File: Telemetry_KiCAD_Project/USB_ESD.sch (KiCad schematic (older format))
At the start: 9 parts

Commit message: Annotated Components
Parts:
- gave numbers to parts that had none: 9
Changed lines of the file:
@@
 $EndDescr
 $Comp
-L dk_USB-DVI-HDMI-Connectors:10118192-0001LF J?
+L dk_USB-DVI-HDMI-Connectors:10118192-0001LF J3
 U 1 1 61A3682F
 P 2500 3450
-F 0 "J?" H 2564 4195 60  0000 C CNN
+F 0 "J3" H 2564 4195 60  0000 C CNN
 F 1 "10118192-0001LF" H 2564 4089 60  0000 C CNN
 F 2 "digikey-footprints:USB_Micro_B_Female_10118192" H 2700 3650 60  0001 L CNN
@@
 $EndComp
 $Comp
-L dk_PMIC-Voltage-Regulators-Linear:LM317T U?
+L dk_PMIC-Voltage-Regulators-Linear:LM317T U6
 U 1 1 61A380E7
 P 5500 3250
-F 0 "U?" H 5500 3537 60  0000 C CNN
+F 0 "U6" H 5500 3537 60  0000 C CNN
 F 1 "LM317T" H 5500 3431 60  0000 C CNN
 F 2 "digikey-footprints:TO-220-3" H 5700 3450 60  0001 L CNN
@@
 $EndComp
 $Comp
-L Device:R_Small R?
+L Device:R_Small R7
 U 1 1 61A38BFA
 P 5500 3800
-F 0 "R?" H 5559 3846 50  0000 L CNN
+F 0 "R7" H 5559 3846 50  0000 L CNN
 F 1 "390Ω" H 5559 3755 50  0000 L CNN
 F 2 "" H 5500 3800 50  0001 C CNN
@@
 $EndComp
 $Comp
-L Device:R_Small R?
+L Device:R_Small R8
 U 1 1 61A38F8D
 P 5900 3450
-F 0 "R?" H 5959 3496 50  0000 L CNN
+F 0 "R8" H 5959 3496 50  0000 L CNN
 F 1 "240Ω" H 5959 3405 50  0000 L CNN
 F 2 "" H 5900 3450 50  0001 C CNN
@@
 $EndComp
 $Comp
-L Device:C_Small C?
+L Device:C_Small C28
 U 1 1 61A3935C
 P 6300 3450
-F 0 "C?" H 6392 3496 50  0000 L CNN
+F 0 "C28" H 6392 3496 50  0000 L CNN
 F 1 "1uF" H 6392 3405 50  0000 L CNN
 F 2 "" H 6300 3450 50  0001 C CNN
@@
 $EndComp
 $Comp
-L Device:C_Small C?
+L Device:C_Small C27
 U 1 1 61A394F0
 P 5000 3500
-F 0 "C?" H 5092 3546 50  0000 L CNN
+F 0 "C27" H 5092 3546 50  0000 L CNN
 F 1 "0.1uF" H 5092 3455 50  0000 L CNN
 F 2 "" H 5000 3500 50  0001 C CNN
@@
 $EndComp
 $Comp
-L power:GND #PWR?
+L power:GND #PWR0140
 U 1 1 61A3A615
 P 6300 3550
-F 0 "#PWR?" H 6300 3300 50  0001 C CNN
+F 0 "#PWR0140" H 6300 3300 50  0001 C CNN
 F 1 "GND" H 6305 3377 50  0000 C CNN
 F 2 "" H 6300 3550 50  0001 C CNN
@@
 $EndComp
 $Comp
-L power:+3.3V #PWR?
+L power:+3.3V #PWR0141
 U 1 1 61A3A807
 P 6100 2950
-F 0 "#PWR?" H 6100 2800 50  0001 C CNN
+F 0 "#PWR0141" H 6100 2800 50  0001 C CNN
 F 1 "+3.3V" H 6115 3123 50  0000 C CNN
 F 2 "" H 6100 2950 50  0001 C CNN
@@
 $EndComp
 $Comp
-L power:GND #PWR?
+L power:GND #PWR0142
 U 1 1 61A3A937
 P 2900 3700
-F 0 "#PWR?" H 2900 3450 50  0001 C CNN
+F 0 "#PWR0142" H 2900 3450 50  0001 C CNN
 F 1 "GND" H 2905 3527 50  0000 C CNN
 F 2 "" H 2900 3700 50  0001 C CNN
@@
 NoConn ~ 2800 3550
 $Comp
-L Device:D_Schottky_Small D?
+L Device:D_Schottky_Small D1
 U 1 1 61A3A235
 P 4700 3250
-F 0 "D?" H 4700 3455 50  0000 C CNN
+F 0 "D1" H 4700 3455 50  0000 C CNN
 F 1 "D_Schottky_Small" H 4700 3364 50  0000 C CNN
 F 2 "" V 4700 3250 50  0001 C CNN
@@
 Connection ~ 5900 3250
 $Comp
-L power:GND #PWR?
+L power:GND #PWR0143
 U 1 1 61A45748
 P 5000 3600
-F 0 "#PWR?" H 5000 3350 50  0001 C CNN
+F 0 "#PWR0143" H 5000 3350 50  0001 C CNN
 F 1 "GND" H 5005 3427 50  0000 C CNN
 F 2 "" H 5000 3600 50  0001 C CNN
@@
 $EndComp
 $Comp
-L power:GND #PWR?
+L power:GND #PWR0144
 U 1 1 61A459EF
 P 5500 3900
-F 0 "#PWR?" H 5500 3650 50  0001 C CNN
+F 0 "#PWR0144" H 5500 3650 50  0001 C CNN
 F 1 "GND" H 5505 3727 50  0000 C CNN
 F 2 "" H 5500 3900 50  0001 C CNN
@@
 	6100 3250 5900 3250
 $Comp
-L power:+5V #PWR?
+L power:+5V #PWR0145
 U 1 1 61A4867E
 P 5000 2950
-F 0 "#PWR?" H 5000 2800 50  0001 C CNN
+F 0 "#PWR0145" H 5000 2800 50  0001 C CNN
 F 1 "+5V" H 5015 3123 50  0000 C CNN
 F 2 "" H 5000 2950 50  0001 C CNN
@@
 	5000 2950 5000 3250
 $Comp
-L Device:Ferrite_Bead_Small FB?
+L Device:Ferrite_Bead_Small FB1
 U 1 1 61A399BC
 P 3800 3250
-F 0 "FB?" V 3563 3250 50  0000 C CNN
+F 0 "FB1" V 3563 3250 50  0000 C CNN
 F 1 "Ferrite_Bead_Small" V 3654 3250 50  0000 C CNN
 F 2 "" V 3730 3250 50  0001 C CNN
@@
 USB_CONN_D-
 $Comp
-L Power_Protection:USBLC6-2SC6 U?
+L Power_Protection:USBLC6-2SC6 U7
 U 1 1 61A51E77
 P 8650 3800
-F 0 "U?" H 8900 4150 50  0000 C CNN
+F 0 "U7" H 8900 4150 50  0000 C CNN
 F 1 "USBLC6-2SC6" H 9000 3500 50  0000 C CNN
 F 2 "Package_TO_SOT_SMD:SOT-23-6" H 7900 4200 50  0001 C CNN
@@
 $EndComp
 $Comp
-L power:+5V #PWR?
+L power:+5V #PWR0146
 U 1 1 61A531CE
 P 8650 3300
-F 0 "#PWR?" H 8650 3150 50  0001 C CNN
+F 0 "#PWR0146" H 8650 3150 50  0001 C CNN
 F 1 "+5V" H 8665 3473 50  0000 C CNN
 F 2 "" H 8650 3300 50  0001 C CNN
@@
 D+
 $Comp
-L power:GND #PWR?
+L power:GND #PWR0147
 U 1 1 61A5476E
 P 8650 4300
-F 0 "#PWR?" H 8650 4050 50  0001 C CNN
+F 0 "#PWR0147" H 8650 4050 50  0001 C CNN
 F 1 "GND" H 8655 4127 50  0000 C CNN
 F 2 "" H 8650 4300 50  0001 C CNN

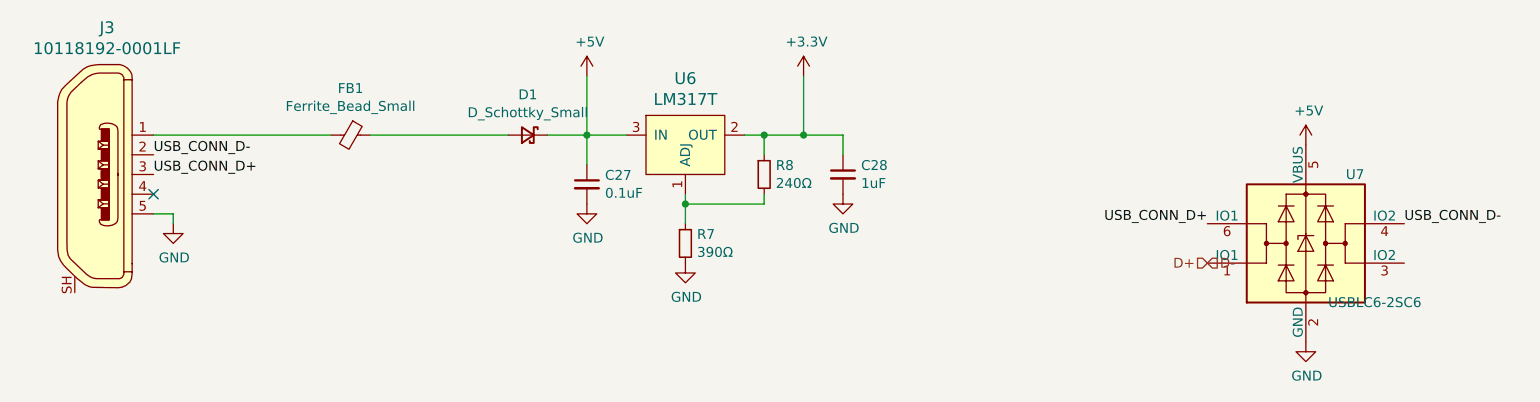
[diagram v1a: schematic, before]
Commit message: Corrected hierarchical pin directions, squashed bugs
There are still some warnings about pins being connected but not driven, don't know how to fix those at the moment
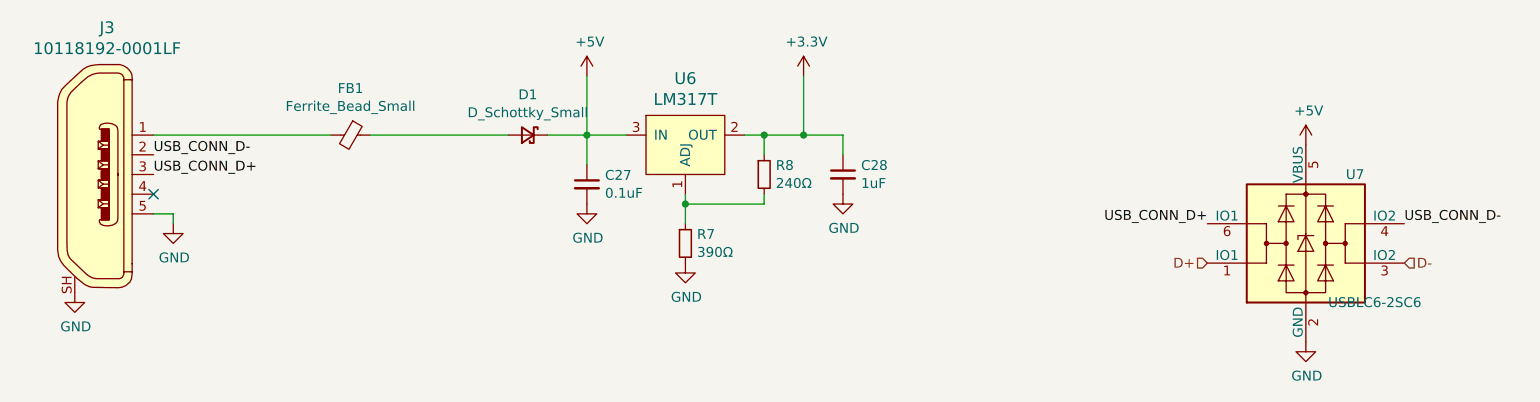
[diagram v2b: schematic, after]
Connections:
- net GND: now also J3.SH
- net D-: now reaches U7.3 (IO2)
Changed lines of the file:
@@
 $Descr A4 11693 8268
 encoding utf-8
-Sheet 8 8
+Sheet 6 8
 Title ""
 Date ""
@@
 Text Label 9150 3700 0    50   ~ 0
 USB_CONN_D-
-Text HLabel 8150 3900 2    50   Input ~ 0
+Text HLabel 9150 3900 2    50   Input ~ 0
 D-
 Text HLabel 8150 3900 0    50   Input ~ 0
@@
 	1    0    0    -1
 $EndComp
+$Comp
+L power:GND #PWR0139
+U 1 1 61A8CA77
+P 2400 4050
+F 0 "#PWR0139" H 2400 3800 50  0001 C CNN
+F 1 "GND" H 2405 3877 50  0000 C CNN
+F 2 "" H 2400 4050 50  0001 C CNN
+F 3 "" H 2400 4050 50  0001 C CNN
+	1    2400 4050
+	1    0    0    -1
+$EndComp

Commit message: Assigned footprints to all components (except duplexer)
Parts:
- C27, C28, FB1: footprint (none) -> Capacitor_SMD:C_0603_1608Metric
- D1: footprint (none) -> Diode_SMD:D_0201_0603Metric
- R7, R8: footprint (none) -> Resistor_SMD:R_0201_0603Metric
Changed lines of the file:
@@
 F 0 "R7" H 5559 3846 50  0000 L CNN
 F 1 "390Ω" H 5559 3755 50  0000 L CNN
-F 2 "" H 5500 3800 50  0001 C CNN
+F 2 "Resistor_SMD:R_0201_0603Metric" H 5500 3800 50  0001 C CNN
 F 3 "~" H 5500 3800 50  0001 C CNN
 	1    5500 3800
@@
 F 0 "R8" H 5959 3496 50  0000 L CNN
 F 1 "240Ω" H 5959 3405 50  0000 L CNN
-F 2 "" H 5900 3450 50  0001 C CNN
+F 2 "Resistor_SMD:R_0201_0603Metric" H 5900 3450 50  0001 C CNN
 F 3 "~" H 5900 3450 50  0001 C CNN
 	1    5900 3450
@@
 F 0 "C28" H 6392 3496 50  0000 L CNN
 F 1 "1uF" H 6392 3405 50  0000 L CNN
-F 2 "" H 6300 3450 50  0001 C CNN
+F 2 "Capacitor_SMD:C_0603_1608Metric" H 6300 3450 50  0001 C CNN
 F 3 "~" H 6300 3450 50  0001 C CNN
 	1    6300 3450
@@
 F 0 "C27" H 5092 3546 50  0000 L CNN
 F 1 "0.1uF" H 5092 3455 50  0000 L CNN
-F 2 "" H 5000 3500 50  0001 C CNN
+F 2 "Capacitor_SMD:C_0603_1608Metric" H 5000 3500 50  0001 C CNN
 F 3 "~" H 5000 3500 50  0001 C CNN
 	1    5000 3500
@@
 F 0 "D1" H 4700 3455 50  0000 C CNN
 F 1 "D_Schottky_Small" H 4700 3364 50  0000 C CNN
-F 2 "" V 4700 3250 50  0001 C CNN
+F 2 "Diode_SMD:D_0201_0603Metric" V 4700 3250 50  0001 C CNN
 F 3 "~" V 4700 3250 50  0001 C CNN
 	1    4700 3250
@@
 F 0 "FB1" V 3563 3250 50  0000 C CNN
 F 1 "Ferrite_Bead_Small" V 3654 3250 50  0000 C CNN
-F 2 "" V 3730 3250 50  0001 C CNN
+F 2 "Capacitor_SMD:C_0603_1608Metric" V 3730 3250 50  0001 C CNN
 F 3 "~" H 3800 3250 50  0001 C CNN
 	1    3800 3250

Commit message: Assigned capacitors for new MCU
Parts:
- U7: symbol Power_Protection:USBLC6-2SC6 -> Telemetry_KiCAD_Project-rescue:USBLC6-2SC6-Power_Protection
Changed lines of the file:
@@
 EESchema Schematic File Version 4
-LIBS:Telemetry_KiCAD_Project-cache
-EELAYER 29 0
+EELAYER 30 0
 EELAYER END
 $Descr A4 11693 8268
@@
 USB_CONN_D-
 $Comp
-L Power_Protection:USBLC6-2SC6 U7
+L Telemetry_KiCAD_Project-rescue:USBLC6-2SC6-Power_Protection U7
 U 1 1 61A51E77
 P 8650 3800
+AR Path="/61A51E77" Ref="U7"  Part="1"
+AR Path="/61A2ED84/61A51E77" Ref="U7"  Part="1"
 F 0 "U7" H 8900 4150 50  0000 C CNN
 F 1 "USBLC6-2SC6" H 9000 3500 50  0000 C CNN

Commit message: PCB Layout Progress
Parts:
- J3: footprint digikey-footprints:USB_Micro_B_Female_10118192 -> Connector_USB:USB_Micro-B_Amphenol_10118194_Horizontal
- U6: footprint digikey-footprints:TO-220-3 -> Package_TO_SOT_SMD:TO-252-3_TabPin2
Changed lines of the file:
@@
 F 0 "J3" H 2564 4195 60  0000 C CNN
 F 1 "10118192-0001LF" H 2564 4089 60  0000 C CNN
-F 2 "digikey-footprints:USB_Micro_B_Female_10118192" H 2700 3650 60  0001 L CNN
+F 2 "Connector_USB:USB_Micro-B_Amphenol_10118194_Horizontal" H 2700 3650 60  0001 L CNN
 F 3 "http://www.amphenol-icc.com/media/wysiwyg/files/drawing/10118192.pdf" H 2700 3750 60  0001 L CNN
 F 4 "609-4613-1-ND" H 2700 3850 60  0001 L CNN "Digi-Key_PN"
@@
 F 0 "U6" H 5500 3537 60  0000 C CNN
 F 1 "LM317T" H 5500 3431 60  0000 C CNN
-F 2 "digikey-footprints:TO-220-3" H 5700 3450 60  0001 L CNN
+F 2 "Package_TO_SOT_SMD:TO-252-3_TabPin2" H 5700 3450 60  0001 L CNN
 F 3 "http://www.st.com/content/ccc/resource/technical/document/datasheet/group1/a0/db/e6/9b/6f/9c/45/7b/CD00000455/files/CD00000455.pdf/jcr:content/translations/en.CD00000455.pdf" H 5700 3550 60  0001 L CNN
 F 4 "497-1575-5-ND" H 5700 3650 60  0001 L CNN "Digi-Key_PN"

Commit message: Added RSD Duplexer Footprint, rearranged RF matching networks
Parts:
- R7, R8: footprint Resistor_SMD:R_0201_0603Metric -> Resistors:0603
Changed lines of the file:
@@
 F 0 "R7" H 5559 3846 50  0000 L CNN
 F 1 "390Ω" H 5559 3755 50  0000 L CNN
-F 2 "Resistor_SMD:R_0201_0603Metric" H 5500 3800 50  0001 C CNN
+F 2 "Resistors:0603" H 5500 3800 50  0001 C CNN
 F 3 "~" H 5500 3800 50  0001 C CNN
 	1    5500 3800
@@
 F 0 "R8" H 5959 3496 50  0000 L CNN
 F 1 "240Ω" H 5959 3405 50  0000 L CNN
-F 2 "Resistor_SMD:R_0201_0603Metric" H 5900 3450 50  0001 C CNN
+F 2 "Resistors:0603" H 5900 3450 50  0001 C CNN
 F 3 "~" H 5900 3450 50  0001 C CNN
 	1    5900 3450

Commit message: Changed USB connector to Molex
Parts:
- J3: footprint Connector_USB:USB_Micro-B_Amphenol_10118194_Horizontal -> Connector_USB:USB_Micro-B_Molex_47346-0001
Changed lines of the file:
@@
 F 0 "J3" H 2564 4195 60  0000 C CNN
 F 1 "10118192-0001LF" H 2564 4089 60  0000 C CNN
-F 2 "Connector_USB:USB_Micro-B_Amphenol_10118194_Horizontal" H 2700 3650 60  0001 L CNN
+F 2 "Connector_USB:USB_Micro-B_Molex_47346-0001" H 2700 3650 60  0001 L CNN
 F 3 "http://www.amphenol-icc.com/media/wysiwyg/files/drawing/10118192.pdf" H 2700 3750 60  0001 L CNN
 F 4 "609-4613-1-ND" H 2700 3850 60  0001 L CNN "Digi-Key_PN"
